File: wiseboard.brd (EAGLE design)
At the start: 80 x 55 mm, 92 parts, among them IC1 MCP73871-2CCI/ML-ND, IC2 LM358MX, Q1 IRLML6402TRPBF, Q2 IRLML6402TRPBF, U1 LT1945EMSPBF, U2 BQ24210DQCT, X1 1528-1438-ND

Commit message: WORK ON NEW CHARGER
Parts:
- added R36, R37: 790, adafruit:R1206
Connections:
- new net N$17: R36.2, U2.2
- new net N$28: R37.2, U2.5
- net GND: now also R36.1, R37.1
- net N$16: now also U2.7
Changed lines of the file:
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@@
 <element name="C9" library="adafruit" package="C1206" value="2u2F" x="-5.842" y="-10.668"/>
 <element name="DONE1" library="adafruit" package="CHIP-LED0805" value="GREEN" x="-11.43" y="-10.414"/>
+<element name="R36" library="adafruit" package="R1206" value="790" x="-11.684" y="-16.764"/>
+<element name="R37" library="adafruit" package="R1206" value="790" x="-11.684" y="-22.86"/>
 </elements>
 <signals>
@@
 <wire x1="21.1119125" y1="36.3048" x2="32.4869125" y2="36.3048" width="0.1524" layer="16"/>
 <wire x1="32.4869125" y1="36.3048" x2="34.1116" y2="34.6801125" width="0.1524" layer="16"/>
-<contactref element="U2" pad="3"/>
 <contactref element="DONE" pad="C"/>
 <contactref element="C9" pad="2"/>
 <contactref element="U2" pad="11"/>
+<contactref element="R36" pad="1"/>
+<contactref element="U2" pad="3"/>
+<contactref element="R37" pad="1"/>
 <wire x1="57.429" y1="32.5685" x2="77.981" y2="21.844" width="0" layer="19" extent="1-1"/>
 <wire x1="55.245" y1="29.0195" x2="57.429" y2="32.5685" width="0" layer="19" extent="1-1"/>
@@
 <wire x1="-5.6007" y1="-3.302" x2="-4.572" y2="-3.302" width="0" layer="19" extent="1-1"/>
 <wire x1="-4.442" y1="-10.668" x2="-4.572" y2="-3.302" width="0" layer="19" extent="1-1"/>
+<wire x1="-13.106" y1="-16.764" x2="-4.442" y2="-10.668" width="0" layer="19" extent="1-1"/>
+<wire x1="-13.106" y1="-22.86" x2="-13.106" y2="-16.764" width="0" layer="19" extent="1-1"/>
 </signal>
 <signal name="VCC">
@@
 <contactref element="U2" pad="6"/>
 <contactref element="DONE1" pad="C"/>
+<contactref element="U2" pad="7"/>
 <wire x1="-3.5433" y1="-4.302" x2="-11.43" y2="-9.364" width="0" layer="19" extent="1-1"/>
+<wire x1="-3.5433" y1="-3.802" x2="-3.5433" y2="-4.302" width="0" layer="19" extent="1-1"/>
+</signal>
+<signal name="N$17">
+<contactref element="U2" pad="2"/>
+<contactref element="R36" pad="2"/>
+<wire x1="-5.6007" y1="-2.802" x2="-10.262" y2="-16.764" width="0" layer="19" extent="1-1"/>
+</signal>
+<signal name="N$28">
+<contactref element="U2" pad="5"/>
+<contactref element="R37" pad="2"/>
+<wire x1="-5.6007" y1="-4.302" x2="-10.262" y2="-22.86" width="0" layer="19" extent="1-1"/>
 </signal>
 </signals>

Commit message: SEMI-FINALIZE NEW CHARGER IC
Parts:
- removed IC1: MCP73871-2CCI/ML-ND, adafruit:QFN20
- removed PWR: RED, adafruit:CHIP-LED0805
- removed R11: 100K, adafruit:M1206
- removed R12: 1K, adafruit:M1206
- removed R15: 1K, adafruit:R1206
- removed R16: 150K, adafruit:R1206
- removed R17: 10K, adafruit:R1206
- removed R18: 2K, adafruit:R1206
- removed R19: 100K, adafruit:R1206
- added JP4: JUMPER, Sparkfun-Passives:SMT-JUMPER_2_NC_PASTE_NO-SILK
- added R38: 7.6k, adafruit:R1206
- POWERGOOD: value GREEN -> BLUE
- R10: value 270K -> 1K
- R37: value 790 -> 10k
- moved R10 60.3 mm to (-11.7, -35.3), turned to 0 degrees
- renumbered DONE1 to POWERGOOD
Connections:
- removed net N$16: POWERGOOD.C, U2.6, U2.7
- removed net N$18: IC1.5, R15.2
- removed net N$19: R15.1, R16.1, R17.1
- removed net N$20: IC1.13, R18.2
- removed net N$21: IC1.12, R19.2
- removed net VBAT1: IC1.14
- removed net VBAT2: IC1.15
- removed net VBAT3: IC1.16
- new net CHARGE_EN: JP4.2, U$12.7, U2.7
- new net N$30: R38.2, U2.4
- net GND: now also JP4.1; no longer IC1.10, IC1.11, R11.1, R16.2, R17.2, R18.1, R19.1
- net N$11: now also POWERGOOD.C, R10.1; no longer PWR.A, R12.2
- net N$28: now also R38.1
- net N$9: now also R10.2, U2.6; no longer IC1.2, R10.1, R11.2
- net VCC: no longer IC1.17, IC1.18, IC1.19, IC1.3, IC1.4, IC1.9, R10.2
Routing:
- net VCC: track 47.7 -> 13.1 mm, vias 3 -> 0
- net N$18: track 30.6 -> 0.00 mm
- net N$21: track 15.7 -> 0.00 mm
- net N$9: track 11.1 -> 0.00 mm
- net N$19: track 6.11 -> 0.00 mm
- net N$20: track 5.80 -> 0.00 mm

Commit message: ROUTE REV 1.5 BOARD
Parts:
- removed CN1: (no value), adafruit:JST-PH-2-SMT-RA
- removed INPUTBUTTONHEADER1, JP2: (no value), pinhead:1X02
- removed R26: 4K7, adafruit:M1206
- removed R27: 10K, adafruit:M1206
- added BAT_CON: (no value), adafruit:JST-PH-2-SMT-RA
- added BAT_PIN: (no value), pinhead:1X02
- moved R10 116.8 mm to (74.0, 44.0)
- moved JP4 115.9 mm to (77.5, 31.6), flipped to the bottom, turned to 180 degrees
- moved POWERGOOD 110.4 mm to (84.0, 45.0), turned to 90 degrees
- moved R38 100.4 mm to (64.0, 37.0), turned to 90 degrees
- moved R36 96.4 mm to (64.0, 43.0), turned to 90 degrees
- moved R37 92.9 mm to (64.0, 31.0), turned to 90 degrees
- moved C9 90.9 mm to (69.0, 41.0)
- moved U2 83.0 mm to (68.0, 37.0)
- moved SOLARPIN 72.7 mm to (83.0, 29.0)
- moved SOLAR 70.1 mm to (83.0, 37.0), turned to 270 degrees
- moved DONE 69.4 mm to (84.0, 49.0)
- moved CHRG/LBO 65.1 mm to (84.0, 47.0)
- moved R14 62.0 mm to (74.0, 48.0), turned to 0 degrees
- moved R13 61.9 mm to (74.0, 52.0), turned to 0 degrees
- moved ESPDEBUG_1 58.1 mm to (6.00, 50.0), turned to 270 degrees
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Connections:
- removed net N$25: D2.C, R22.1, U$14.1
- new net N$16: C11.1, U$11.15, U$11.16
- net +3V3: no longer INPUTBUTTONHEADER1.1
- net ADC: no longer R26.1, R27.2
- net GND: now also BAT_CON.2, BAT_PIN.2; no longer CN1.2, JP2.2, R27.1
- net N$26: no longer INPUTBUTTONHEADER1.2
- net VBAT: now also BAT_CON.1, BAT_PIN.1; no longer CN1.1, JP2.1
- net VCC: now also D2.C, R22.1, U$14.1
- net VDD: no longer C11.1, R26.2, U$11.15, U$11.16
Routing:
- net VDD: track 178.3 -> 76.8 mm, vias 15 -> 6
- net +22V: track 158.1 -> 61.7 mm, vias 12 -> 4
- net CHARGE_EN: track 0.00 -> 77.8 mm, vias 0 -> 2
- net CL: track 122.3 -> 45.4 mm
- net N$1: track 88.3 -> 12.0 mm, vias 4 -> 0
- net BOOSTENA: track 132.0 -> 57.5 mm, vias 5 -> 0
- net NFB1: track 82.0 -> 13.5 mm, vias 5 -> 0
- net QP3: track 82.8 -> 19.2 mm, vias 4 -> 2
- net N$26: track 173.2 -> 111.2 mm, vias 7 -> 1
- net -15V: track 132.9 -> 71.1 mm, vias 8 -> 2
- net N$3: track 70.9 -> 14.2 mm, vias 2 -> 0
- net N$16: track 0.00 -> 55.3 mm
- net OE: track 105.4 -> 52.2 mm
- net N$25: track 50.3 -> 0.00 mm, vias 4 -> 0
- net TXD: track 52.9 -> 11.3 mm
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- added copper zone on layer 16, net GND
- removed copper zone on layer 16, net N$12
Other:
- board size 80 x 55 mm -> 87 x 67 mm
- board text added: "+"
- board text added: "0"
- board text added: "12"
- board text added: "13"
- board text added: "14"
- board text added: "15"
- board text added: "16"
- board text added: "3V3"
- board text added: "ADC"
- board text added: "BATTERY"
- board text added: "BOOT"
- board text added: "B_EN"
- board text added: "CHRG"
- board text added: "CH_PD"
- board text added: "CL"
- board text added: "DONE"
- board text added: "EN TO GND"
- board text added: "GND"
- board text added: "GPIO0"
- board text added: "OE"
- board text added: "PANEL"
- board text added: "PWRG"
- board text added: "RST"
- board text added: "RST to 16"
- board text added: "RXD"
- board text added: "TXD"
- board text added: "test"

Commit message: SEMI-FINALIZE PCB DECALS
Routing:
- net N$26: track 111.2 -> 115.0 mm
- net CHARGE_EN: track 77.8 -> 79.4 mm
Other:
- board text added: "Board by"
- board text added: "Project WISE"
- board text added: "Rev 1.6"
- board text removed: "test"

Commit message: FINALIZE PCB DECALS
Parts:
- moved BAT_CON 1.50 mm to (50.0, 63.5)
- moved R37 0.50 mm to (64.5, 31.0)
- moved S3 0.28 mm to (71.0, 21.5)
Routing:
- net VBAT: track 118.5 -> 125.0 mm
- net RESET: track 94.7 -> 98.8 mm, vias 1 -> 3
- net GND: track 135.4 -> 138.9 mm
- net POSEN: track 58.6 -> 59.9 mm
- net N$27: track 44.5 -> 45.5 mm, vias 0 -> 2
- net +3V3: track 272.8 -> 271.9 mm, vias 3 -> 7

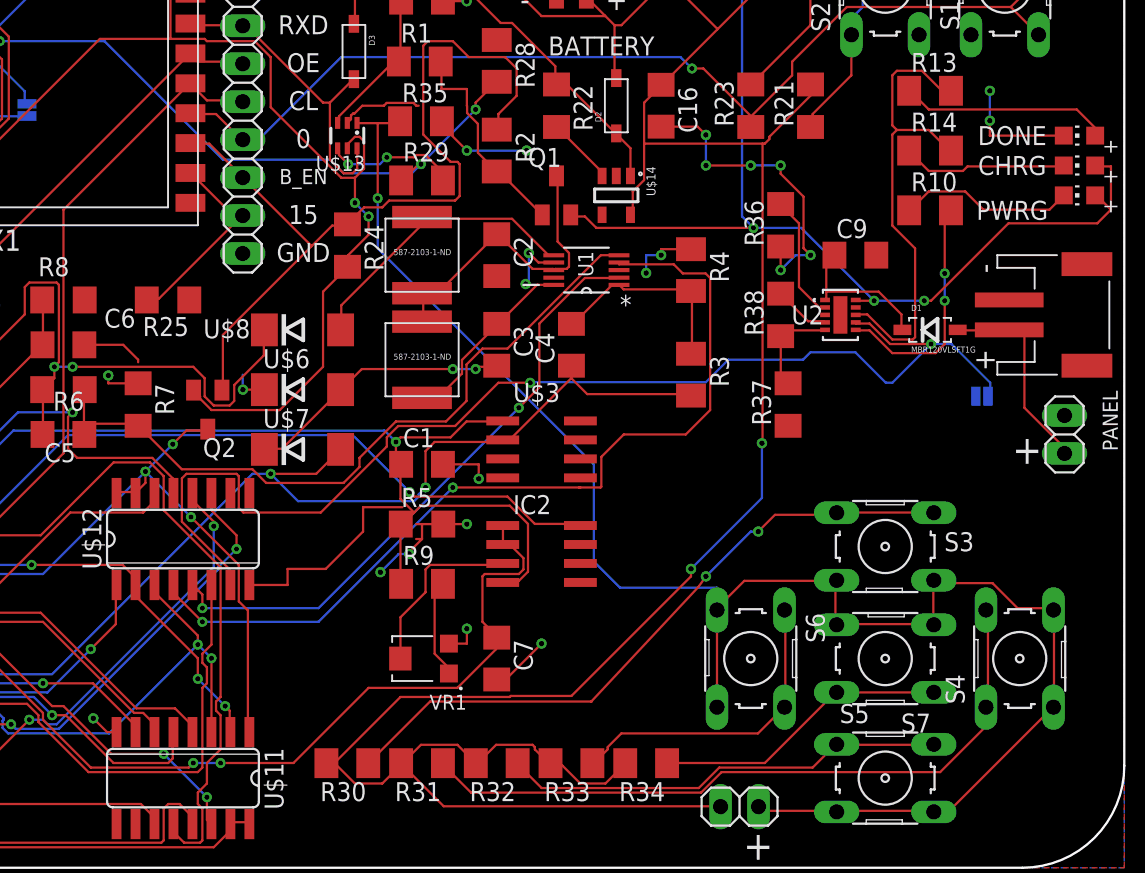
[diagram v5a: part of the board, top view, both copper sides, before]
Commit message: ADD W25Q32JV TO PCB AND ROUTE
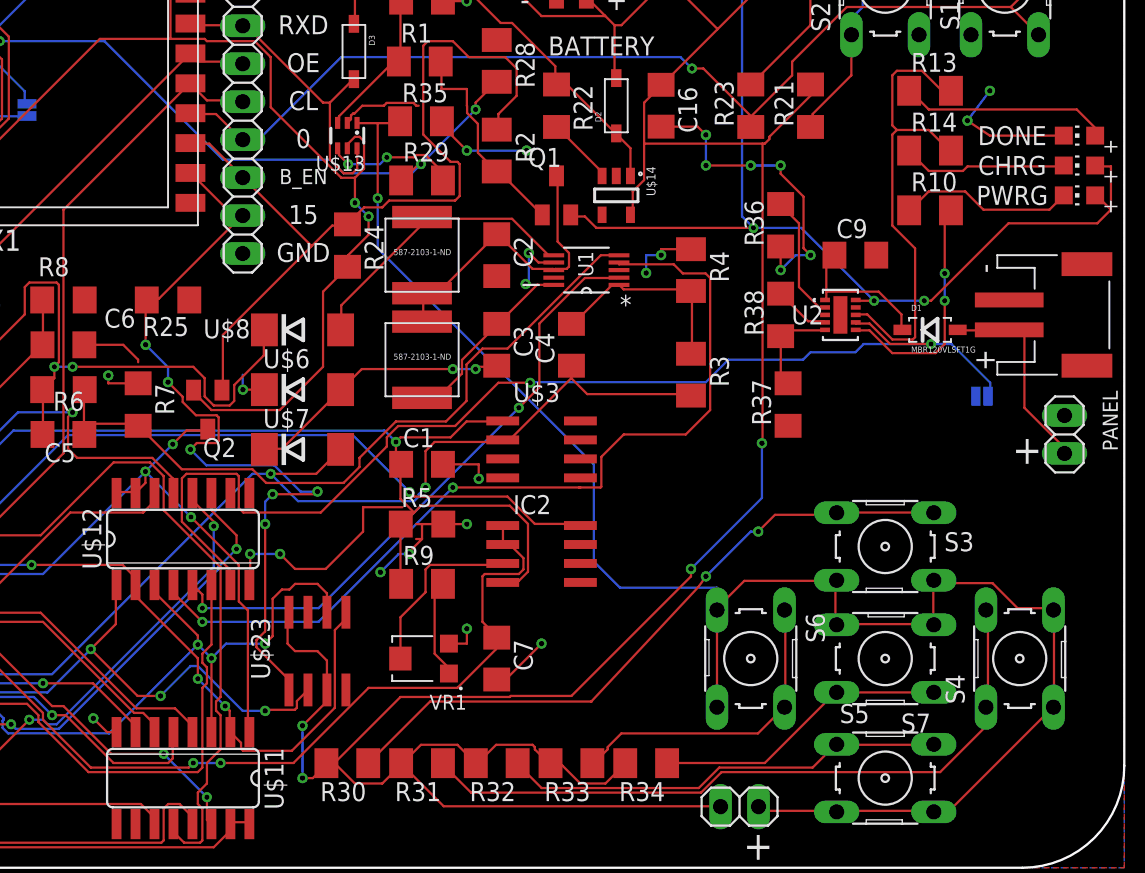
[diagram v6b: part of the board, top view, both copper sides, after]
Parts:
- added U$23: W25Q32JVSSIQ, WISE:SO8
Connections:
- net +3V3: now also U$23.3, U$23.8
- net GND: now also U$23.4
- net GPIO12: now also U$23.2
- net GPIO13: now also U$23.5
- net GPIO14: now also U$23.6
- net GPIO15: now also U$23.1
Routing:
- net GPIO15: track 13.6 -> 55.3 mm, vias 0 -> 6
- net GPIO12: track 82.5 -> 101.3 mm, vias 1 -> 3
- net +3V3: track 271.9 -> 287.7 mm, vias 7 -> 9
- net GPIO13: track 63.6 -> 79.2 mm
- net GPIO14: track 94.9 -> 107.6 mm, vias 2 -> 3
- net GND: track 138.9 -> 141.5 mm, vias 36 -> 38
- net CHARGE_EN: track 79.4 -> 78.7 mm

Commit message: FINAL REV1.5 PCB LAYOUT
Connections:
- removed net N$16: C11.1, U$11.15, U$11.16
- removed net N$24: R29.2, U$13.4
- new net N$12: R28.2, U$13.4
- net ADC: now also R28.1, R29.2; no longer R28.2, R29.1
- net CHARGE_EN: no longer U$12.7
- net GND: now also R29.1; no longer R28.1
- net VDD: now also C11.1, U$11.15, U$11.16
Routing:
- net CHARGE_EN: track 78.7 -> 11.2 mm, vias 2 -> 1
- net VDD: track 76.8 -> 139.3 mm, vias 6 -> 8
- net N$16: track 55.3 -> 0.00 mm
- net ADC: track 47.8 -> 80.5 mm
- net N$12: track 0.00 -> 14.0 mm, vias 0 -> 2
- net N$24: track 8.99 -> 0.00 mm, vias 2 -> 0
- net QP7@2: track 36.4 -> 38.6 mm
- net QP6@2: track 40.5 -> 41.7 mm
